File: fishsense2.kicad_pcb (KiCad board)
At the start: 4 copper layers, 83.2 x 73.7 mm, 100 parts, among them J1 Conn_02x10_Odd_Even, J2 BATT_OUT, J3 BATT_IN, J4 Barrel_Jack_Switch, J6 USB_C_Receptacle, J7 USB3_A, J8 USB3_A, K1 UMS05-1A80-75L, Q1 Q_NMOS_DGS, Q2 Q_NMOS_DSG, SW1 SW_Reed, SW2 SW_Reed, U1 TPS62821DLC, U2 TUSB8020BIPHP, U3 HD3SS3220, U4 TPS62821DLC, U5 P783F-Q24-S5-S, Y1 Crystal

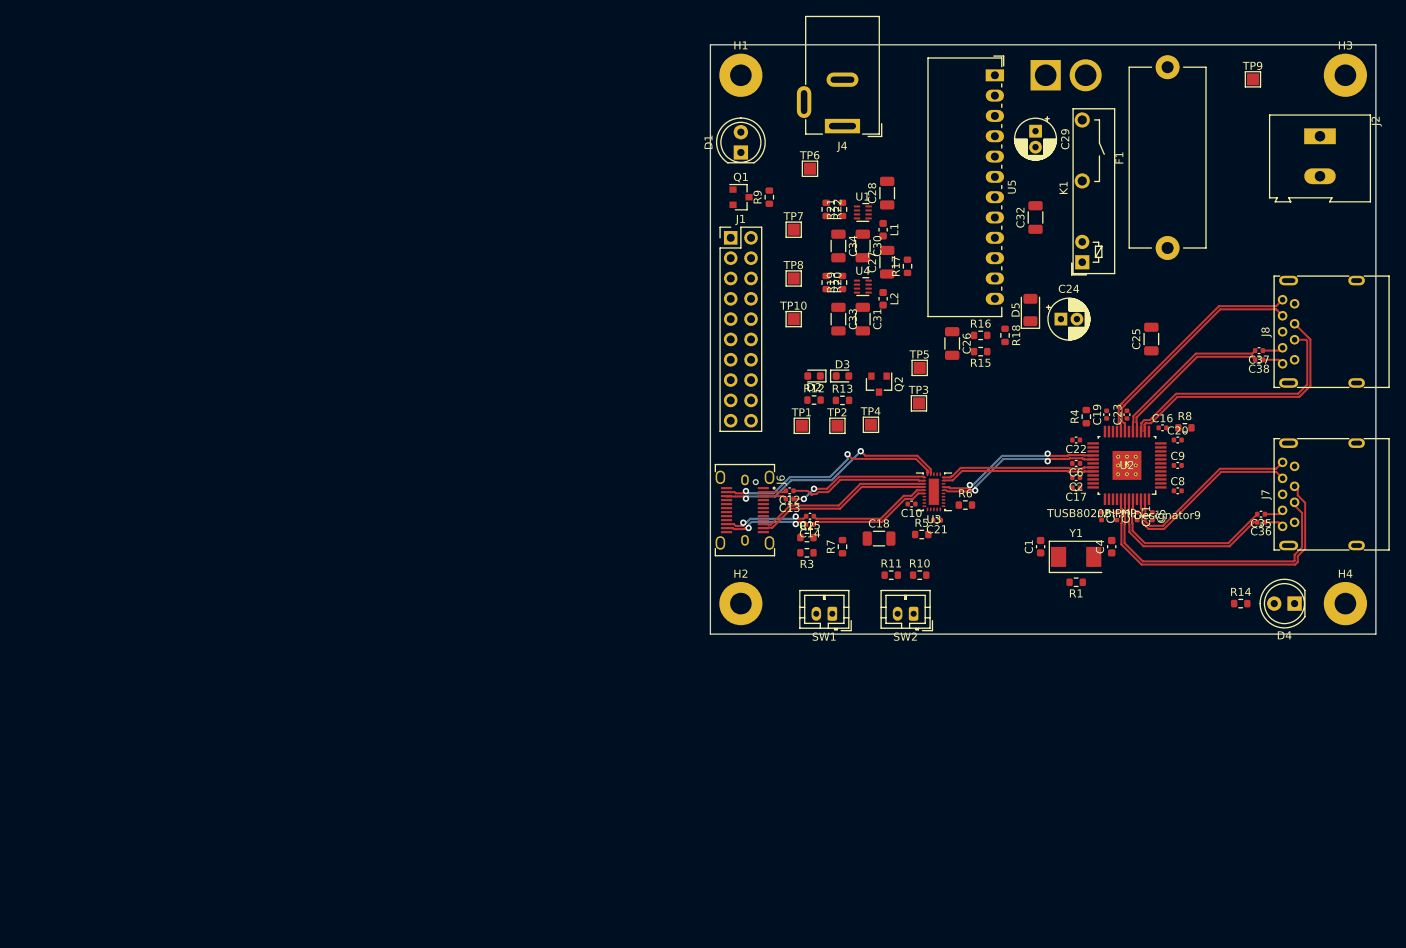
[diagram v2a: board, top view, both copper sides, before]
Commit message: Updated footprints. Placed components and added silkscreen.
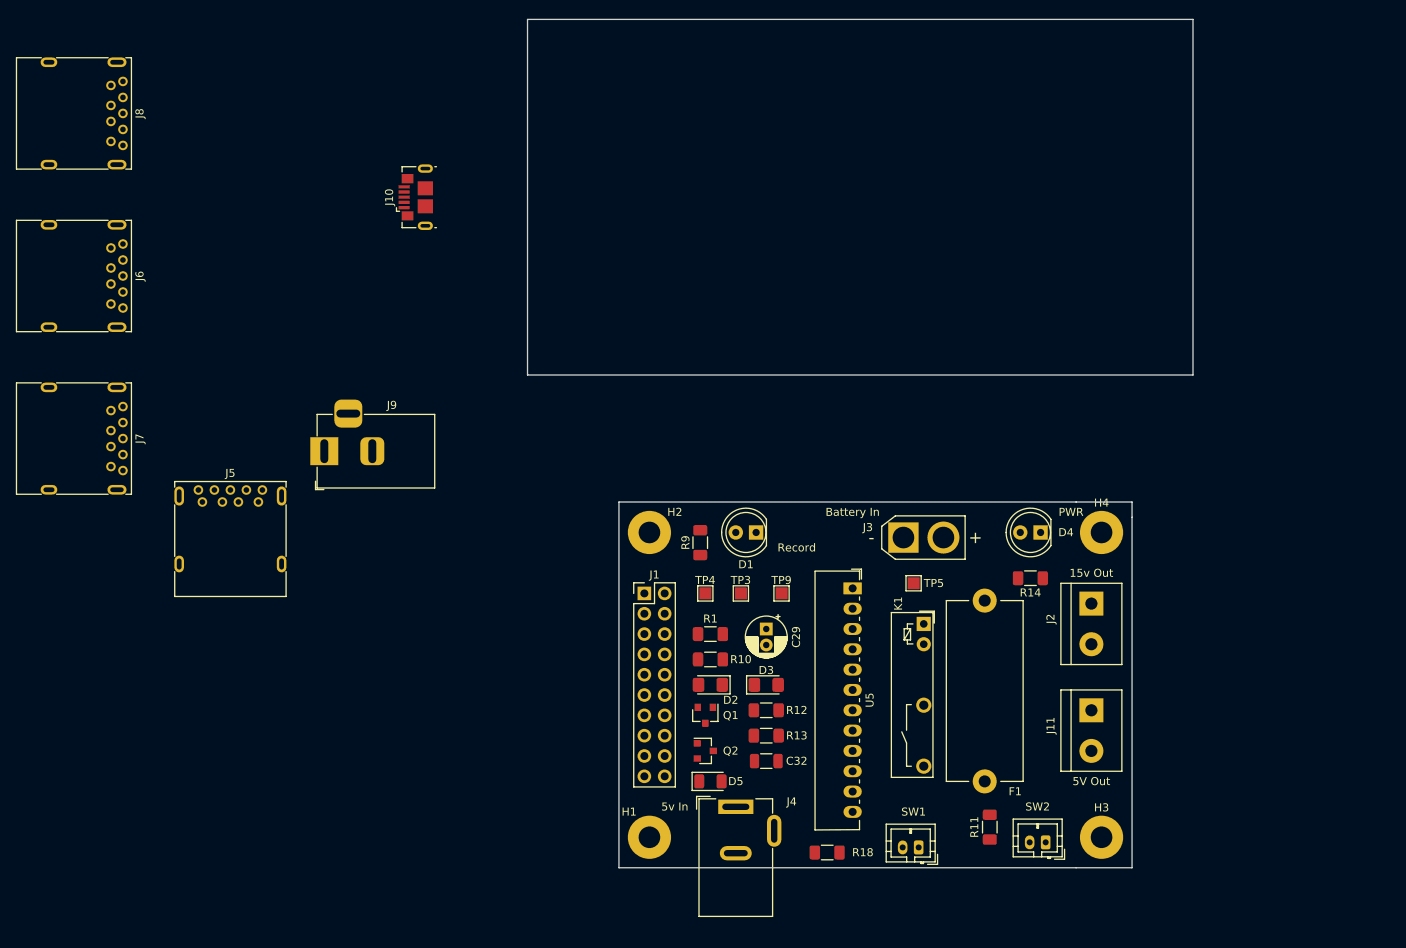
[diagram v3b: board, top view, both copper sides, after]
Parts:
- removed C1, C4: 18p, Capacitor_SMD:C_0603_1608Metric
- removed C10, C12, C13, C14, C15, C21: 100n, Capacitor_SMD:C_0402_1005Metric
- removed C11, C16, C17, C19, C2, C20, C22, C23, C3, C35, C36, C37, C38, C5, C6, C7, C8, C9: 0.1u, Capacitor_SMD:C_0402_1005Metric
- removed C18, C30, C31, C33, C34: 10u, Capacitor_SMD:C_1206_3216Metric
- removed C24: 100u, Capacitor_THT:CP_Radial_D5.0mm_P2.00mm
- removed C25: 1u, Capacitor_SMD:C_1206_3216Metric
- removed C26: 0.47u, Capacitor_SMD:C_1206_3216Metric
- removed C27, C28: 4.7u, Capacitor_SMD:C_1206_3216Metric
- removed L1, L2: 0.47u, Inductor_SMD:L_0603_1608Metric
- removed R15: 30k, Resistor_SMD:R_0603_1608Metric
- removed R16: 20k, Resistor_SMD:R_0603_1608Metric
- removed R17: 50k, Resistor_SMD:R_0603_1608Metric
- removed R19: 470k, Resistor_SMD:R_0603_1608Metric
- removed R2: 90k, Resistor_SMD:R_0603_1608Metric
- removed R20, R22: 100k, Resistor_SMD:R_0603_1608Metric
- removed R21: 82k, Resistor_SMD:R_0603_1608Metric
- removed R3: 10k, Resistor_SMD:R_0603_1608Metric
- removed R4: 9k53, Resistor_SMD:R_0603_1608Metric
- removed R5: 200k, Resistor_SMD:R_0603_1608Metric
- removed R6: 4.7k, Resistor_SMD:R_0603_1608Metric
- removed R7: 900k, Resistor_SMD:R_0603_1608Metric
- removed R8: 1k, Resistor_SMD:R_0603_1608Metric
- removed TP1: CC1, TestPoint:TestPoint_Pad_1.5x1.5mm
- removed TP10: 3.3v, TestPoint:TestPoint_Pad_1.5x1.5mm
- removed TP2: CC2, TestPoint:TestPoint_Pad_1.5x1.5mm
- removed TP6: 1.1v EN, TestPoint:TestPoint_Pad_1.5x1.5mm
- removed TP7: 3.3v EN, TestPoint:TestPoint_Pad_1.5x1.5mm
- removed TP8: 1.1v, TestPoint:TestPoint_Pad_1.5x1.5mm
- removed U1, U4: TPS62821DLC, Package_DFN_QFN:Texas_VSON-HR-8_1.5x2mm_P0.5mm
- removed U2: TUSB8020BIPHP, fishsense2:TUSB8020BIPHP
- removed U3: HD3SS3220, fishsense2:TI_VQFN_RNH
- removed Y1: Crystal, Crystal:Crystal_SMD_0603-2Pin_6.0x3.5mm
- added J10: USB_B_Micro, Connector_USB:USB_Micro-B_GCT_USB3076-30-A, F.Cu at (91.4, 73.7)
- added J11: Screw_Terminal_01x02, TerminalBlock:TerminalBlock_bornier-2_P5.08mm, F.Cu at (175.9, 137.8)
- added J5: USB3_A, Connector_USB:USB3_A_Molex_48393-001, F.Cu at (64.8, 111.8)
- added J9: Barrel_Jack, Connector_BarrelJack:BarrelJack_Horizontal, F.Cu at (80.0, 105.4)
- D2, D3: footprint Diode_SMD:D_0603_1608Metric -> Diode_SMD:D_1206_3216Metric_Pad1.42x1.75mm_HandSolder
- J2: footprint TerminalBlock:TerminalBlock_Altech_AK300-2_P5.00mm -> TerminalBlock:TerminalBlock_bornier-2_P5.08mm
- J3: moved to F.Cu
- J6: value USB_C_Receptacle -> USB3_A; footprint Connector_USB:USB_C_Receptacle_JAE_DX07S024WJ1R350 -> Connector_USB:USB3_A_Molex_48393-001
- R1: value 1M -> 39k; footprint Resistor_SMD:R_0603_1608Metric -> Resistor_SMD:R_1206_3216Metric_Pad1.30x1.75mm_HandSolder
- R10, R11, R12, R13, R14, R18, R9: footprint Resistor_SMD:R_0603_1608Metric -> Resistor_SMD:R_1206_3216Metric_Pad1.30x1.75mm_HandSolder
- moved J8 151.9 mm to (53.3, 59.7), turned to 270 degrees
- moved J7 148.6 mm to (53.3, 100.3), turned to 270 degrees
- moved H3 100.0 mm to (177.2, 153.7)
- moved H1 95.9 mm to (120.7, 153.7)
- moved TP9 87.2 mm to (137.2, 123.2)
- moved J4 86.1 mm to (131.4, 149.9), turned to 0 degrees
- moved J6 85.8 mm to (53.3, 80.0)
- moved C32 75.8 mm to (135.3, 144.1), turned to 180 degrees
- moved D5 71.2 mm to (128.3, 146.7), turned to 0 degrees
- moved C29 70.7 mm to (135.3, 127.6)
- moved F1 70.5 mm to (162.6, 146.7)
- moved R18 68.4 mm to (142.9, 155.6), turned to 180 degrees
- moved U5 66.6 mm to (146.1, 122.6)
- moved J2 65.0 mm to (175.9, 124.5)
- moved Q1 64.9 mm to (127.6, 138.4), turned to 270 degrees
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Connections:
- D2 pad 2: REED -> Net-(D2-Pad2)
- J7 pad 1: +5V -> Net-(J7-Pad1)
- J7 pad 10: GND -> Net-(J7-Pad10)
- J7 pad 2: /D_DN1_N -> Net-(J7-Pad2)
- J7 pad 3: /D_DN1_P -> Net-(J7-Pad3)
- J7 pad 4: GND -> Net-(J7-Pad4)
- J7 pad 5: /RX_DN1_N -> Net-(J7-Pad5)
- J7 pad 6: /RX_DN1_P -> Net-(J7-Pad6)
- J7 pad 7: GND -> Net-(J7-Pad7)
- J7 pad 8: /TX_DN1_F_N -> Net-(J7-Pad8)
- J7 pad 9: /TX_DN1_F_P -> Net-(J7-Pad9)
- J8 pad 1: +5V -> Net-(J8-Pad1)
- J8 pad 10: GND -> Net-(J8-Pad10)
- J8 pad 2: /D_DN2_N -> Net-(J8-Pad2)
- J8 pad 3: /D_DN2_P -> Net-(J8-Pad3)
- J8 pad 4: GND -> Net-(J8-Pad4)
- J8 pad 5: /RX_DN2_N -> Net-(J8-Pad5)
- J8 pad 6: /RX_DN2_P -> Net-(J8-Pad6)
- J8 pad 7: GND -> Net-(J8-Pad7)
- J8 pad 8: /TX_DN2_F_N -> Net-(J8-Pad8)
- J8 pad 9: /TX_DN2_F_P -> Net-(J8-Pad9)
- R1 pad 1: /XO -> Net-(D2-Pad2)
- R1 pad 2: /XI -> REED
- SW2 pad 1: REED -> Net-(D2-Pad2)
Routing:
- net /D_DN1_P: track 39.3 -> 0.00 mm
- net /D_DN1_N: track 35.8 -> 0.00 mm
- net /D_DN2_P: track 32.2 -> 0.00 mm
- net /D_DN2_N: track 30.9 -> 0.00 mm
- net /RX1_N: track 29.7 -> 0.00 mm, vias 2 -> 0
- net /RX_DN2_N: track 29.3 -> 0.00 mm
- net /RX1_P: track 29.2 -> 0.00 mm, vias 2 -> 0
- net /RX_DN2_P: track 28.7 -> 0.00 mm
- net /RX_DN1_P: track 24.1 -> 0.00 mm
- net /RX_DN1_N: track 23.5 -> 0.00 mm
- net /RX2_P: track 22.3 -> 0.00 mm
- net /RX2_N: track 22.3 -> 0.00 mm
- net /TX_DN1_P: track 22.1 -> 0.00 mm
- net /TX_DN1_N: track 21.7 -> 0.00 mm
- net /TX_P: track 21.0 -> 0.00 mm, vias 2 -> 0
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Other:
- board size 83.2 x 73.7 mm -> 83.2 x 106 mm
- board text added: "15v Out"
- board text added: "5V Out"
- board text added: "5v In"
- board text added: "Battery In"
- board text added: "PWR"
- board text added: "Record"

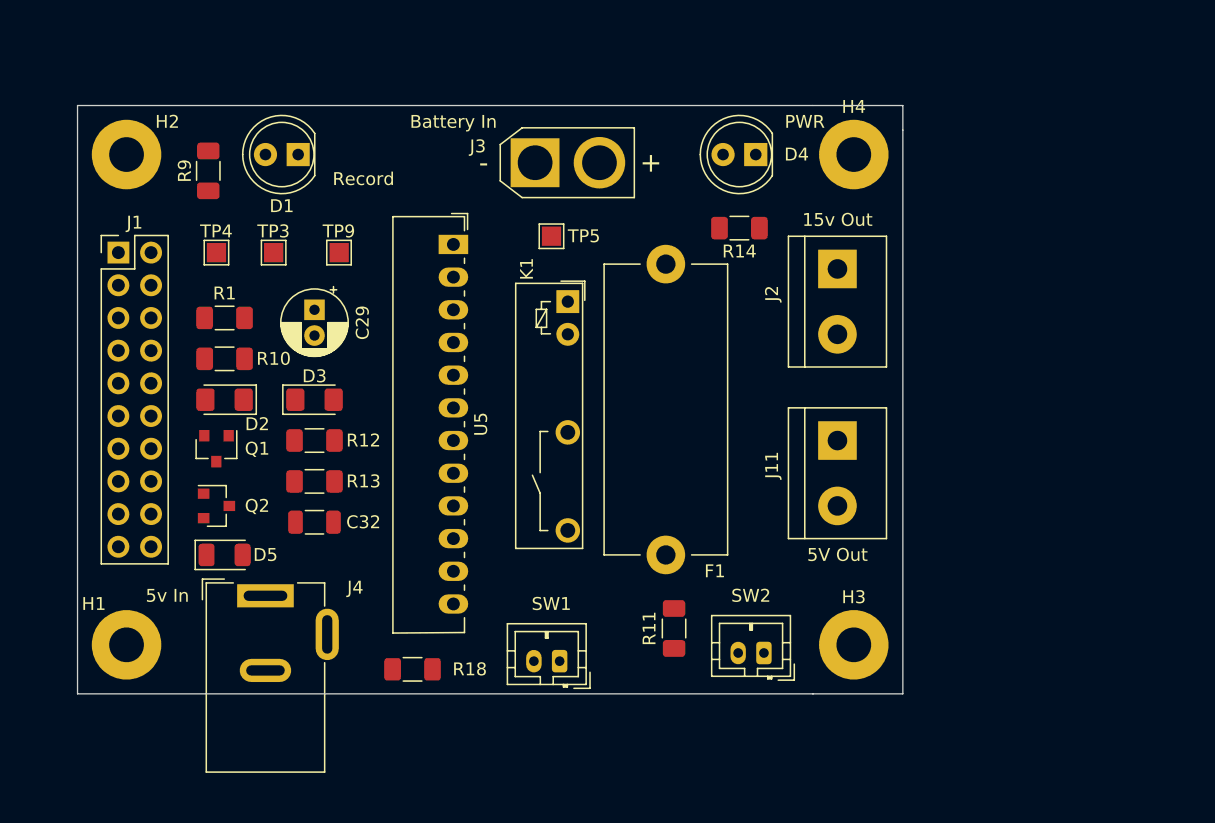
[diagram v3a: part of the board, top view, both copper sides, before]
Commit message: Changed footprints to right angle versions. Adjusted board outline to orbitty carrier size.
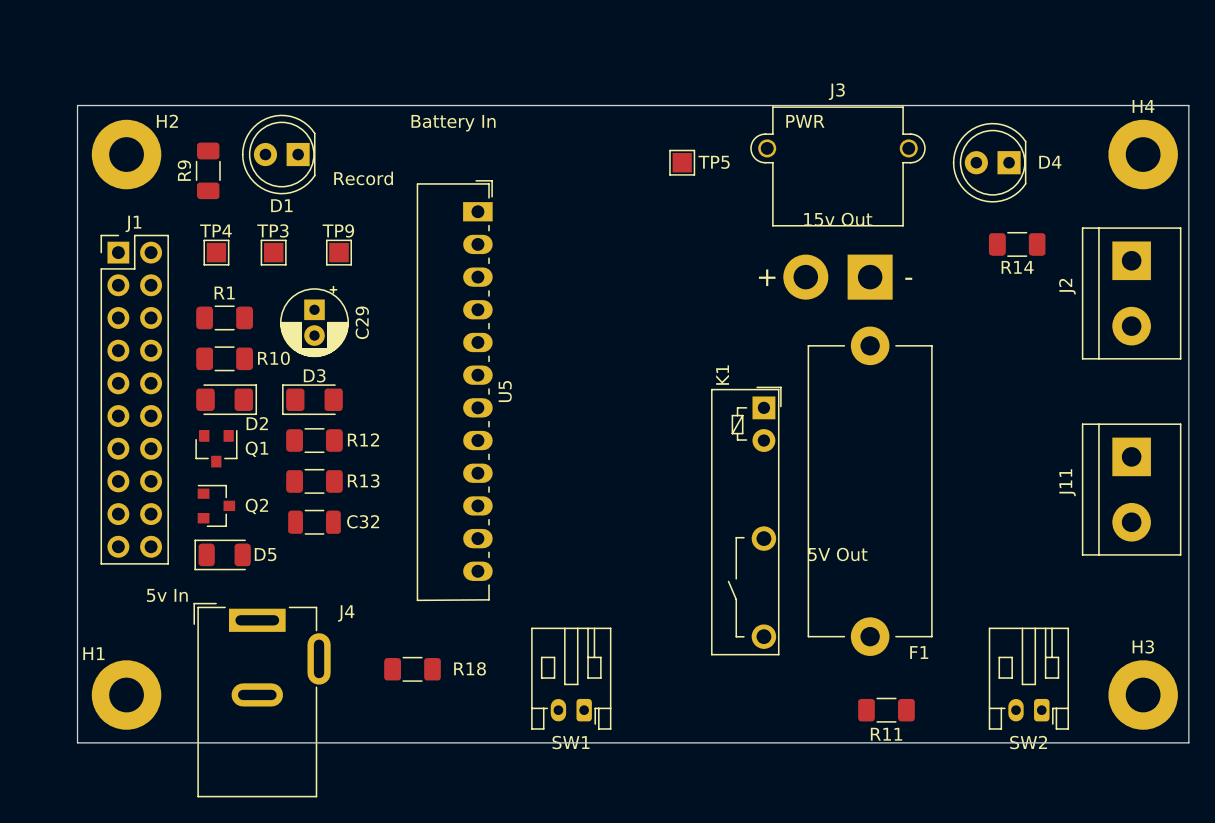
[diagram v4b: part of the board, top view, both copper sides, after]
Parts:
- J3: footprint Connector_AMASS:AMASS_XT30U-F_1x02_P5.0mm_Vertical -> Connector_AMASS:AMASS_XT30PW-M_1x02_P2.50mm_Horizontal
- SW1, SW2: footprint Connector_JST:JST_PH_B2B-PH-K_1x02_P2.00mm_Vertical -> Connector_JST:JST_PH_S2B-PH-K_1x02_P2.00mm_Horizontal
- moved J3 27.5 mm to (178.4, 125.1)
- moved J11 22.9 mm to (198.8, 139.1)
- moved J2 22.9 mm to (198.8, 123.8)
- moved H3 22.8 mm to (199.7, 157.6)
- moved H4 22.5 mm to (199.7, 115.6)
- moved SW2 22.0 mm to (191.8, 158.8)
- moved R14 21.6 mm to (189.9, 122.6)
- moved D4 19.7 mm to (189.2, 116.2)
- moved R11 17.7 mm to (179.7, 158.8), turned to 0 degrees
- moved K1 17.3 mm to (170.2, 135.3)
- moved F1 17.1 mm to (178.4, 153.0)
- moved TP5 11.7 mm to (163.8, 116.2)
- moved SW1 4.26 mm to (156.2, 158.8)
- moved H1 3.90 mm to (120.7, 157.6)
- moved U5 3.18 mm to (148.0, 120.0)
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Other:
- board size 83.2 x 106 mm -> 97.8 x 109.9 mm

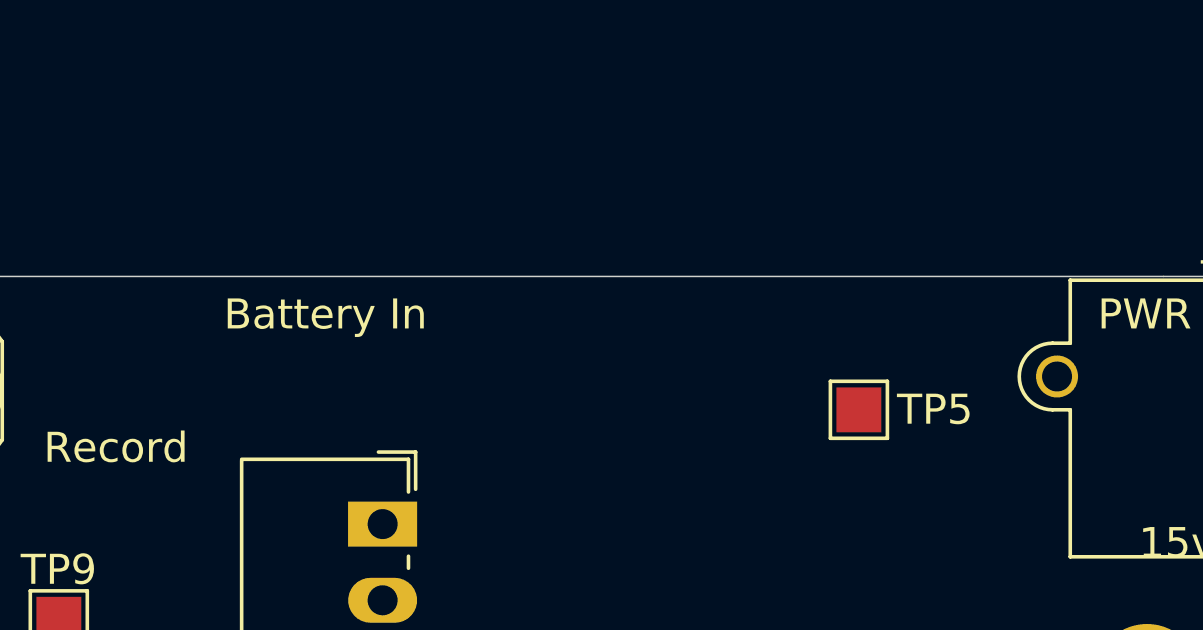
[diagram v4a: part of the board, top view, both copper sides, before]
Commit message: Added battery undervoltage protection, needs consideration as to whether it would work.
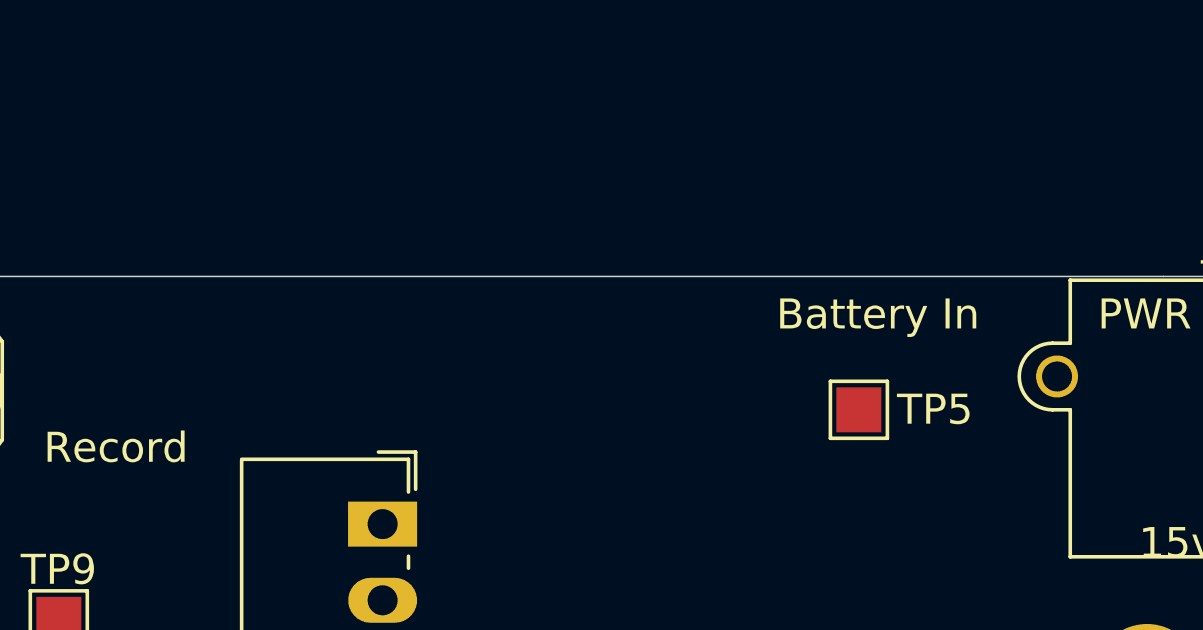
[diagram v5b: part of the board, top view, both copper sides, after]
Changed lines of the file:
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@@
     (effects (font (size 1 1) (thickness 0.15)))
   )
-  (gr_text "Battery In" (at 146.05 113.03) (layer F.SilkS)
+  (gr_text "Battery In" (at 164.465 113.03) (layer F.SilkS)
     (effects (font (size 1 1) (thickness 0.15)))
   )
